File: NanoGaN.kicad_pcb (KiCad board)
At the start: 6 copper layers, 54 x 94 mm, 221 parts, among them J1 U_DC, J10 Conn_01x06, J11 Conn_01x04, J12 USB4085-GF-A, J14 Conn_01x03, J2 GND, J3 Phase_U, J4 Phase_V, J5 Phase_W, J6 FTSH-107-01-L-DV-K-TR, J7 Conn_01x03, J8 Conn_01x02, J9 Conn_01x07, Q1 IGC025S08S1, Q2 IGC025S08S1, Q3 IGC025S08S1, Q4 IGC025S08S1, Q5 IGC025S08S1, Q6 IGC025S08S1, Q7 Si2302CDS, U1 STM32H723VGTx, U10 SN74LVC1G66DCKR, U11 SN74LVC1G66DCKR, U12 LMG1205YFXR, U13 BMI323, U14 AS5047P-ATST, U15 TCAN1044VDRQ1, U16 SN74LVC1G66DCKR, U17 AD8418, U18 SN74LVC1G66DCKR, U19 NCS2220AMUT1G, U2 LMR51635XDDCR, U20 NCS2220AMUT1G, U21 NCS2220AMUT1G, U3 AMS1117, U4 AD8418, U5 LMG1205YFXR, U6 SN74LVC1G66DCKR, U7 SN74LVC1G66DCKR, U8 LMG1205YFXR, U9 AD8418, X1 8MHz

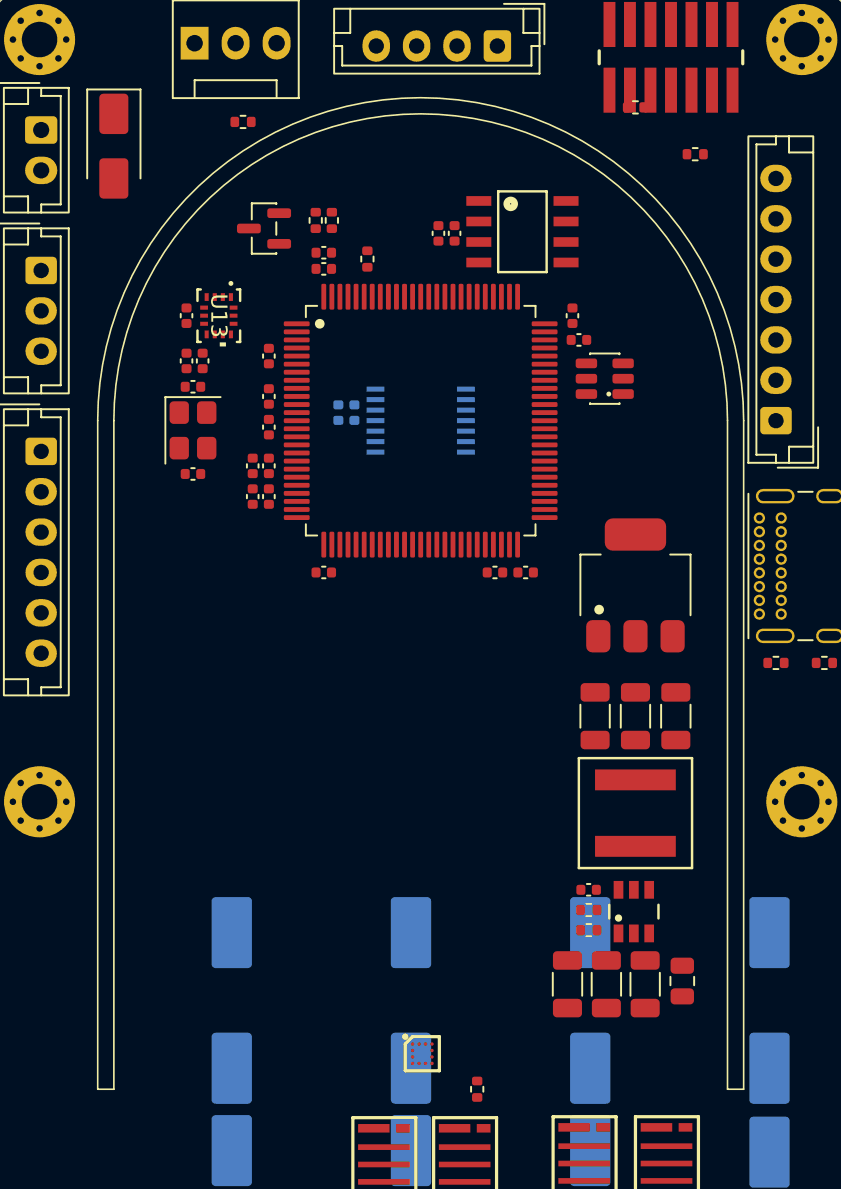
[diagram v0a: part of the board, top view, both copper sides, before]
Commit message: added cooling channel symbol, footprint and 3D model
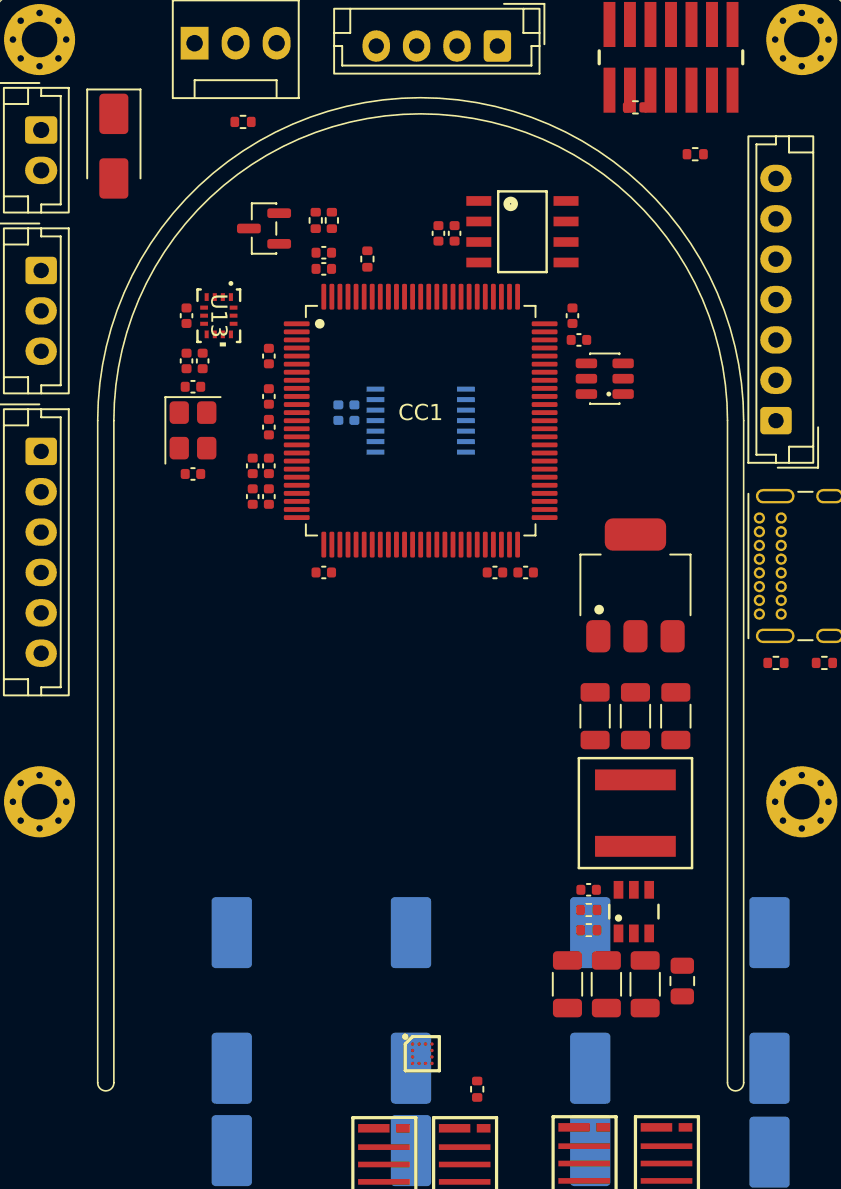
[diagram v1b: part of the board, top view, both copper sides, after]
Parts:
- added CC1: ~, NanoGaN:CoolingChannel, F.Cu at (145.2, 75.0)
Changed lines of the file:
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@@
 		)
 	)
+	(footprint "NanoGaN:CoolingChannel"
+		(layer "F.Cu")
+		(at 145.1651 75)
+		(property "Reference" "CC1"
+			(at 0 -0.5 0)
+			(unlocked yes)
+			(layer "F.SilkS")
+			(effects
+				(font
+					(size 1 1)
+					(thickness 0.1)
+				)
+			)
+		)
+		(property "Value" "~"
+			(at 0 1 0)
+			(unlocked yes)
+			(layer "F.Fab")
+			(effects
+				(font
+					(size 1 1)
+					(thickness 0.15)
+				)
+			)
+		)
+		(property "Datasheet" ""
+			(at 0 0 0)
+			(unlocked yes)
+			(layer "F.Fab")
+			(hide yes)
+			(effects
+				(font
+					(size 1 1)
+					(thickness 0.15)
+				)
+			)
+		)
+		(property "Description" ""
+			(at 0 0 0)
+			(unlocked yes)
+			(layer "F.Fab")
+			(hide yes)
+			(effects
+				(font
+					(size 1 1)
+					(thickness 0.15)
+				)
+			)
+		)
+		(sheetname "/Power/")
+		(sheetfile "power.kicad_sch")
+		(attr smd)
+		(fp_line
+			(start -20 0)
+			(end -20 41)
+			(stroke
+				(width 0.1)
+				(type solid)
+			)
+			(layer "F.SilkS")
+		)
+		(fp_line
+			(start -19 0)
+			(end -19 41)
+			(stroke
+				(width 0.1)
+				(type solid)
+			)
+			(layer "F.SilkS")
+		)
+		(fp_line
+			(start 19 0)
+			(end 19 41)
+			(stroke
+				(width 0.1)
+				(type solid)
+			)
+			(layer "F.SilkS")
+		)
+		(fp_line
+			(start 20 0)
+			(end 20 41)
+			(stroke
+				(width 0.1)
+				(type solid)
+			)
+			(layer "F.SilkS")
+		)
+		(fp_arc
+			(start -20 0)
+			(mid 0 -20)
+			(end 20 0)
+			(stroke
+				(width 0.1)
+				(type solid)
+			)
+			(layer "F.SilkS")
+		)
+		(fp_arc
+			(start -19 0)
+			(mid 0 -19)
+			(end 19 0)
+			(stroke
+				(width 0.1)
+				(type solid)
+			)
+			(layer "F.SilkS")
+		)
+		(fp_arc
+			(start -19 41)
+			(mid -19.5 41.5)
+			(end -20 41)
+			(stroke
+				(width 0.1)
+				(type default)
+			)
+			(layer "F.SilkS")
+		)
+		(fp_arc
+			(start 20 41)
+			(mid 19.5 41.5)
+			(end 19 41)
+			(stroke
+				(width 0.1)
+				(type default)
+			)
+			(layer "F.SilkS")
+		)
+		(fp_text user "${REFERENCE}"
+			(at 0 2.5 0)
+			(unlocked yes)
+			(layer "F.Fab")
+			(effects
+				(font
+					(size 1 1)
+					(thickness 0.15)
+				)
+			)
+		)
+		(embedded_fonts no)
+		(model "${KIPRJMOD}/NanoGaN_3D_models/cc_v3.step"
+			(offset
+				(xyz -23.5 23.5 -0.5)
+			)
+			(scale
+				(xyz 1 1 1)
+			)
+			(rotate
+				(xyz -0 -0 -0)
+			)
+		)
+	)
 	(footprint "Capacitor_SMD:C_0402_1005Metric"
 		(layer "F.Cu")
@@
 		)
 	)
-	(gr_line
-		(start 165.1651 75)
-		(end 165.1651 116.4)
-		(stroke
-			(width 0.1)
-			(type default)
-		)
-		(layer "F.SilkS")
-	)
-	(gr_line
-		(start 164.1651 116.4)
-		(end 165.1651 116.4)
-		(stroke
-			(width 0.1)
-			(type default)
-		)
-		(layer "F.SilkS")
-	)
-	(gr_arc
-		(start 126.1651 75)
-		(mid 145.1651 56)
-		(end 164.1651 75)
-		(stroke
-			(width 0.1)
-			(type solid)
-		)
-		(layer "F.SilkS")
-	)
-	(gr_arc
-		(start 125.1651 75)
-		(mid 145.1651 55)
-		(end 165.1651 75)
-		(stroke
-			(width 0.1)
-			(type solid)
-		)
-		(layer "F.SilkS")
-	)
-	(gr_line
-		(start 126.1651 75)
-		(end 126.1651 116.4)
-		(stroke
-			(width 0.1)
-			(type solid)
-		)
-		(layer "F.SilkS")
-	)
-	(gr_line
-		(start 126.1651 116.4)
-		(end 125.1651 116.4)
-		(stroke
-			(width 0.1)
-			(type default)
-		)
-		(layer "F.SilkS")
-	)
-	(gr_line
-		(start 164.1651 75)
-		(end 164.1651 116.4)
-		(stroke
-			(width 0.1)
-			(type default)
-		)
-		(layer "F.SilkS")
-	)
-	(gr_line
-		(start 125.1651 75)
-		(end 125.1651 116.4)
-		(stroke
-			(width 0.1)
-			(type solid)
-		)
-		(layer "F.SilkS")
-	)
 	(gr_arc

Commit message: added the first draft of the layout
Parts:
- removed C102, C104: 1u, Capacitor_SMD:C_0402_1005Metric
- removed C103, C105: 100n, Capacitor_SMD:C_0402_1005Metric
- removed C96, C97, C98, C99: 1n, Capacitor_SMD:C_0201_0603Metric
- removed R28: 1m, NanoGaN:RES_00FEA_VIS-L
- removed R30, R32: 10k, Resistor_SMD:R_0603_1608Metric
- removed R7: 10k, Resistor_SMD:R_0402_1005Metric
- removed U10, U11, U16, U18: SN74LVC1G66DCKR, NanoGaN:DCK5
- removed U17, U9: AD8418, Package_SO:SOIC-8_3.9x4.9mm_P1.27mm
- added C67: 100n, Capacitor_SMD:C_0805_2012Metric, F.Cu at (152.7, 134.9)
- added C68: 1u, Capacitor_SMD:C_1206_3216Metric, F.Cu at (167.7, 128.1)
- added MH7: M3, MountingHole:MountingHole_3.2mm_M3_Pad_Via, F.Cu at (168.8, 142.6)
- C100: value 1u -> 100n
- C11, C12, C13, C14, C27, C35: value 150u -> 470u; footprint Capacitor_SMD:CP_Elec_10x10.5 -> Capacitor_THT:CP_Radial_D12.5mm_P5.00mm
- C18, C36, C85, C87: footprint Capacitor_SMD:C_0201_0603Metric -> Capacitor_SMD:C_0402_1005Metric
- C24, C25, C33, C38, C89: moved to B.Cu
- C26: value 1u -> 100n; moved to B.Cu
- C28, C39, C91: value 1n -> 100p; footprint Capacitor_SMD:C_0201_0603Metric -> Capacitor_SMD:C_0402_1005Metric; moved to B.Cu
- C37: value 1u -> 4u7
- C40: value 15n -> 4u7
- C44, C81: value 150u -> 100n; footprint Capacitor_SMD:CP_Elec_10x10.5 -> Capacitor_SMD:C_0805_2012Metric; moved to F.Cu
- C50: footprint Capacitor_SMD:C_0402_1005Metric -> Capacitor_SMD:C_0805_2012Metric
- C88: value 1u -> 100n; footprint Capacitor_SMD:C_0402_1005Metric -> Capacitor_SMD:C_0805_2012Metric
- C90: value 15n -> 100n; footprint Capacitor_SMD:C_0402_1005Metric -> Capacitor_SMD:C_0805_2012Metric
- C92: value 15n -> 100n
- J1: value U_DC -> XT60-M; footprint TerminalBlock_Wuerth:Wuerth_REDCUBE-THR_WP-THRBU_74650073_THR -> NanoGaN:AMASS_XT60-M
- J2: value GND -> XT60-M; footprint TerminalBlock_Wuerth:Wuerth_REDCUBE-THR_WP-THRBU_74650073_THR -> NanoGaN:AMASS_XT60-M
- MH1, MH2, MH3, MH4, MH5, MH6: value M2 -> M3; footprint MountingHole:MountingHole_2.2mm_M2_Pad_Via -> MountingHole:MountingHole_3.2mm_M3_Pad_Via
- R11, R21: value 1m -> 10k; footprint NanoGaN:RES_00FEA_VIS-L -> Resistor_SMD:R_0402_1005Metric
- U4: value AD8418 -> ACS37030LLZATR-065B3; footprint Package_SO:SOIC-8_3.9x4.9mm_P1.27mm -> NanoGaN:ACS37030LLZATR020B3; moved to B.Cu
- U6, U7: value SN74LVC1G66DCKR -> ACS37030LLZATR-065B3; footprint NanoGaN:DCK5 -> NanoGaN:ACS37030LLZATR020B3; moved to B.Cu
- moved U12 148.0 mm to (131.4, 126.1), turned to 90 degrees
- moved R5 147.7 mm to (151.5, 139.0)
- moved C18 145.7 mm to (151.5, 138.0)
- moved R23 143.3 mm to (129.3, 128.4), turned to -90 degrees
- moved C91 141.8 mm to (121.9, 132.3), turned to 90 degrees
- moved R4 141.2 mm to (151.0, 141.0), turned to 90 degrees
- moved R25 140.3 mm to (130.3, 128.4), turned to 90 degrees
- moved R22 140.1 mm to (134.4, 128.4), turned to -90 degrees
- moved C41 140.0 mm to (128.3, 126.1), turned to -90 degrees
- moved R27 139.9 mm to (136.4, 139.0)
- moved R24 139.6 mm to (132.4, 128.4), turned to 90 degrees
- moved Q6 139.3 mm to (127.9, 132.8), turned to -90 degrees
- moved Q5 139.2 mm to (133.0, 132.8), turned to -90 degrees
- moved C89 139.2 mm to (123.7, 129.5), turned to 180 degrees
- moved C43 138.1 mm to (129.3, 126.1), turned to -90 degrees
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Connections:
- net /MCU/BOOT0 renamed BOOT0
- C100 pad 1: +3V3A -> +3V3
- C101 pad 1: +3V3A -> +3V3
- C24 pad 1: +3V3A -> +3V3
- C24 pad 2: AGND -> PGND
- C25 pad 1: Net-(U16-A) -> /HalfBridgeU/I_CURR_SENS-
- C25 pad 2: /HalfBridgeU/U_PHASE_SENS -> PGND
- C26 pad 1: +3V3A -> /HalfBridgeV/I_CURR_SENS-
- C26 pad 2: AGND -> PGND
- C28 pad 1: /HalfBridgeU/I_CURR_SENS -> /HalfBridgeU/I_CURR_SENS+
- C28 pad 2: AGND -> PGND
- C33 pad 1: Net-(U7-A) -> /HalfBridgeW/I_CURR_SENS-
- C33 pad 2: /HalfBridgeV/U_PHASE_SENS -> PGND
- C37 pad 1: +3V3A -> +3V3
- C37 pad 2: AGND -> GND
- C38 pad 1: +3V3A -> +3V3
- C38 pad 2: AGND -> PGND
- C39 pad 1: /HalfBridgeV/I_CURR_SENS -> /HalfBridgeV/I_CURR_SENS+
- C39 pad 2: AGND -> PGND
- C40 pad 1: /HalfBridgeV/I_CURR_SENS -> +3V3
- C40 pad 2: Net-(U10-A) -> GND
- C50 pad 1: Net-(U11-A) -> U_DC
- C50 pad 2: /HalfBridgeW/U_PHASE_SENS -> PGND
- C88 pad 1: +3V3A -> U_DC
- C88 pad 2: AGND -> PGND
- C89 pad 1: +3V3A -> +3V3
- C89 pad 2: AGND -> PGND
- C90 pad 1: /HalfBridgeU/I_CURR_SENS -> U_DC
- C90 pad 2: Net-(U6-A) -> PGND
- C91 pad 1: /HalfBridgeW/I_CURR_SENS -> /HalfBridgeW/I_CURR_SENS+
- C91 pad 2: AGND -> PGND
- C92 pad 1: /HalfBridgeW/I_CURR_SENS -> +3V3
- C92 pad 2: Net-(U18-A) -> AGND
- C95 pad 1: /HalfBridgeU/DAC_OCP_P -> /HalfBridgeU/DAC_OCP_N
- MH3 pad 1: PGND -> GND
- R11 pad 1: /HalfBridgeU/HS -> /Connectors/EXT_TEMP2
- R11 pad 2: /HalfBridgeU/PHASE -> GND
- R21 pad 1: /HalfBridgeV/HS -> /Connectors/EXT_TEMP1
- R21 pad 2: /HalfBridgeV/PHASE -> GND
- U1 pad 22: unconnected-(U1-PA0-Pad22) -> /HalfBridgeU/U_PHASE_SENS
- U1 pad 23: unconnected-(U1-PA1-Pad23) -> /HalfBridgeV/U_PHASE_SENS
- U1 pad 24: unconnected-(U1-PA2-Pad24) -> /HalfBridgeW/U_PHASE_SENS
- U1 pad 30: /HalfBridgeW/I_CURR_SENS -> /HalfBridgeU/I_CURR_SENS+
- U1 pad 31: /HalfBridgeW/U_PHASE_SENS -> /HalfBridgeU/I_CURR_SENS-
- U1 pad 32: /HalfBridgeV/U_PHASE_SENS -> /HalfBridgeV/I_CURR_SENS+
- U1 pad 33: /HalfBridgeV/I_CURR_SENS -> /HalfBridgeV/I_CURR_SENS-
- U1 pad 34: /HalfBridgeU/I_CURR_SENS -> /HalfBridgeW/I_CURR_SENS-
- U1 pad 35: /HalfBridgeU/U_PHASE_SENS -> /HalfBridgeW/I_CURR_SENS+
- U1 pad 37: /HalfBridgeU/EN_FILTER_I -> unconnected-(U1-PE7-Pad37)
- U1 pad 7: unconnected-(U1-PC13-Pad7) -> /Connectors/HALL1
- U1 pad 8: unconnected-(U1-PC14-Pad8) -> /Connectors/HALL2
- U1 pad 81: FDCAN1_RX -> /MCU/UART4_RX
- U1 pad 82: FDCAN1_TX -> /MCU/UART4_TX
- U1 pad 83: FDCAN1_STB -> unconnected-(U1-PD2-Pad83)
- U1 pad 85: unconnected-(U1-PD4-Pad85) -> FDCAN1_STB
- U1 pad 9: unconnected-(U1-PC15-Pad9) -> /Connectors/HALL3
- U1 pad 90: /Connectors/SERVO -> unconnected-(U1-PB4(NJTRST)-Pad90)
- U1 pad 91: /Connectors/SERVO -> unconnected-(U1-PB5-Pad91)
- U1 pad 92: /Connectors/VCP_RX -> unconnected-(U1-PB6-Pad92)
- U1 pad 93: /Connectors/VCP_TX -> unconnected-(U1-PB7-Pad93)
- U1 pad 95: unconnected-(U1-PB8-Pad95) -> FDCAN1_RX
- U1 pad 96: /Connectors/FAN_PWM -> FDCAN1_TX
- U13 pad 1: SPI4_MISO -> SPI2_MISO
- U13 pad 12: SPI4_NSS -> SPI2_NSS
- U13 pad 13: SPI4_SCK -> SPI2_SCK
- U13 pad 14: SPI4_MOSI -> SPI2_MOSI
- U14 pad 1: SPI2_NSS -> SPI4_NSS
- U14 pad 2: SPI2_SCK -> SPI4_SCK
- U14 pad 3: SPI2_MISO -> SPI4_MISO
- U14 pad 4: SPI2_MOSI -> SPI4_MOSI
- U19 pad 2: /HalfBridgeU/I_CURR_SENS -> /HalfBridgeU/I_CURR_SENS+
- U19 pad 6: /HalfBridgeU/I_CURR_SENS -> /HalfBridgeU/I_CURR_SENS+
- U19 pad 8: +3V3A -> +3V3
- U20 pad 2: /HalfBridgeV/I_CURR_SENS -> /HalfBridgeV/I_CURR_SENS+
- U20 pad 6: /HalfBridgeV/I_CURR_SENS -> /HalfBridgeV/I_CURR_SENS+
- U20 pad 8: +3V3A -> +3V3
- U21 pad 2: /HalfBridgeW/I_CURR_SENS -> /HalfBridgeW/I_CURR_SENS+
- U21 pad 6: /HalfBridgeW/I_CURR_SENS -> /HalfBridgeW/I_CURR_SENS+
- U21 pad 8: +3V3A -> +3V3
- U4 pad 1: /HalfBridgeU/PHASE -> /HalfBridgeU/HS
- U4 pad 2: AGND -> /HalfBridgeU/PHASE
- U4 pad 3: AGND -> PGND
- U4 pad 4: unconnected-(U4-NC-Pad4) -> /HalfBridgeU/I_CURR_SENS-
- U4 pad 5: /HalfBridgeU/I_CURR_SENS -> /HalfBridgeU/I_CURR_SENS+
- U4 pad 6: +3V3A -> +3V3
- U6 pad 1: Net-(U6-A) -> /HalfBridgeV/HS
- U6 pad 2: AGND -> /HalfBridgeV/PHASE
- U6 pad 4: /HalfBridgeU/EN_FILTER_I -> /HalfBridgeV/I_CURR_SENS-
- U6 pad 5: +3V3A -> /HalfBridgeV/I_CURR_SENS+
- U7 pad 1: Net-(U7-A) -> /HalfBridgeW/HS
- U7 pad 2: PGND -> /HalfBridgeW/PHASE
- U7 pad 4: /HalfBridgeU/EN_FILTER_U -> /HalfBridgeW/I_CURR_SENS-
- U7 pad 5: +3V3A -> /HalfBridgeW/I_CURR_SENS+
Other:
- board size 54 x 94 mm -> 60 x 100 mm
- board text added: "JLCJLCJLC"

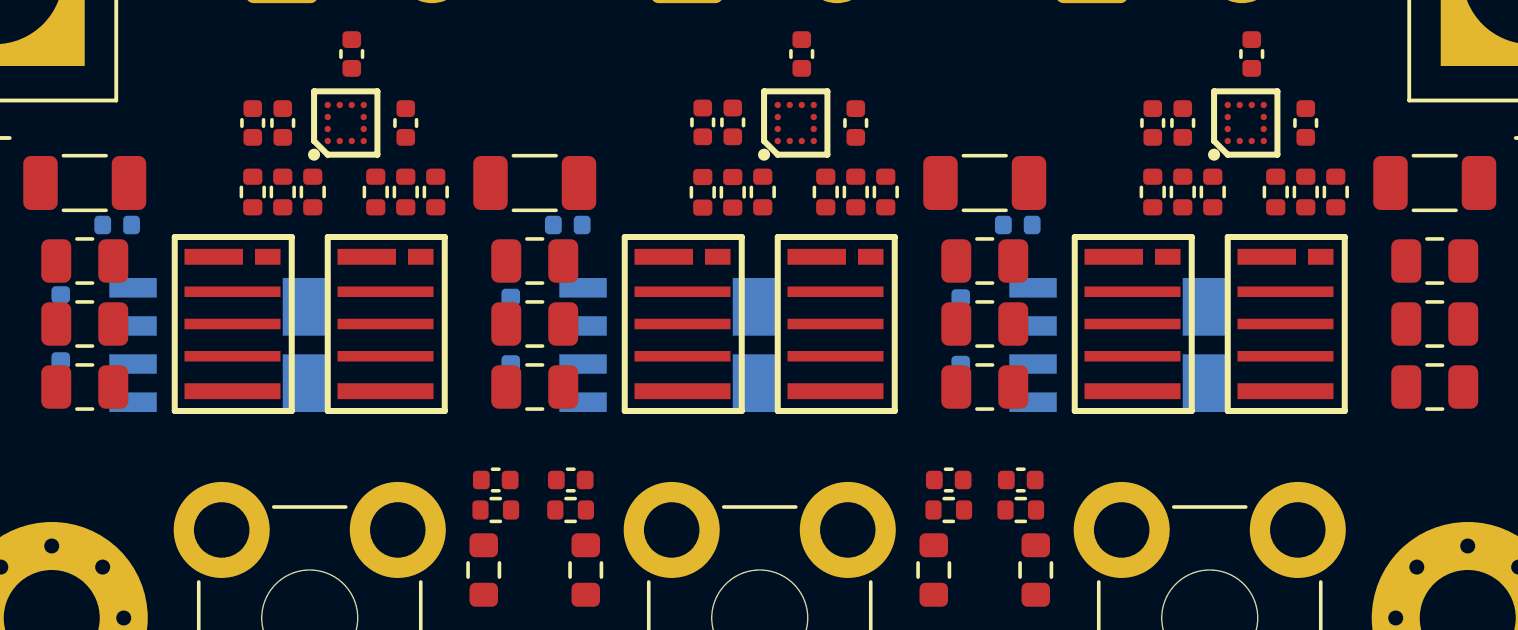
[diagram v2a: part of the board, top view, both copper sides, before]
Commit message: added heatsinks and updated cooling channel
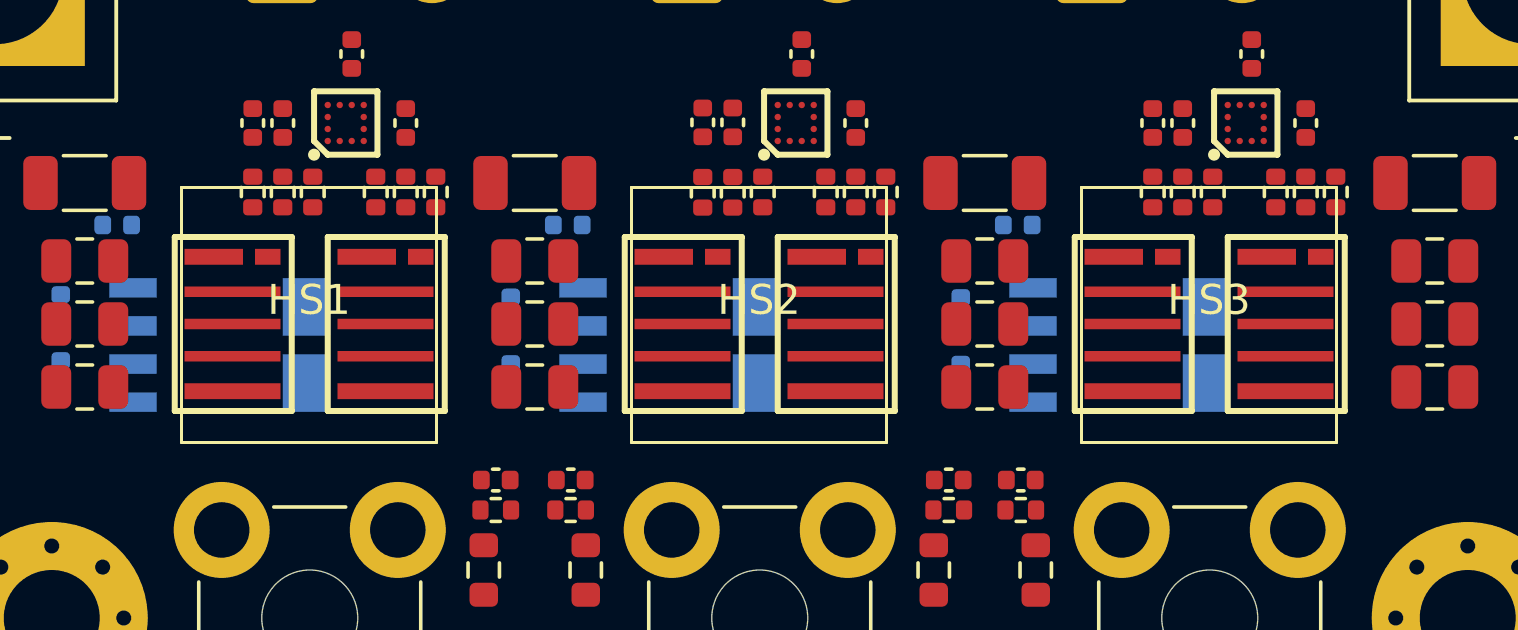
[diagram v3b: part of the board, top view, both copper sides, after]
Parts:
- added HS1: Heatsink, NanoGaN:HSB01-080808, F.Cu at (130.1, 132.5)
- added HS2: Heatsink, NanoGaN:HSB01-080808, F.Cu at (145.1, 132.5)
- added HS3: Heatsink, NanoGaN:HSB01-080808, F.Cu at (160.1, 132.5)

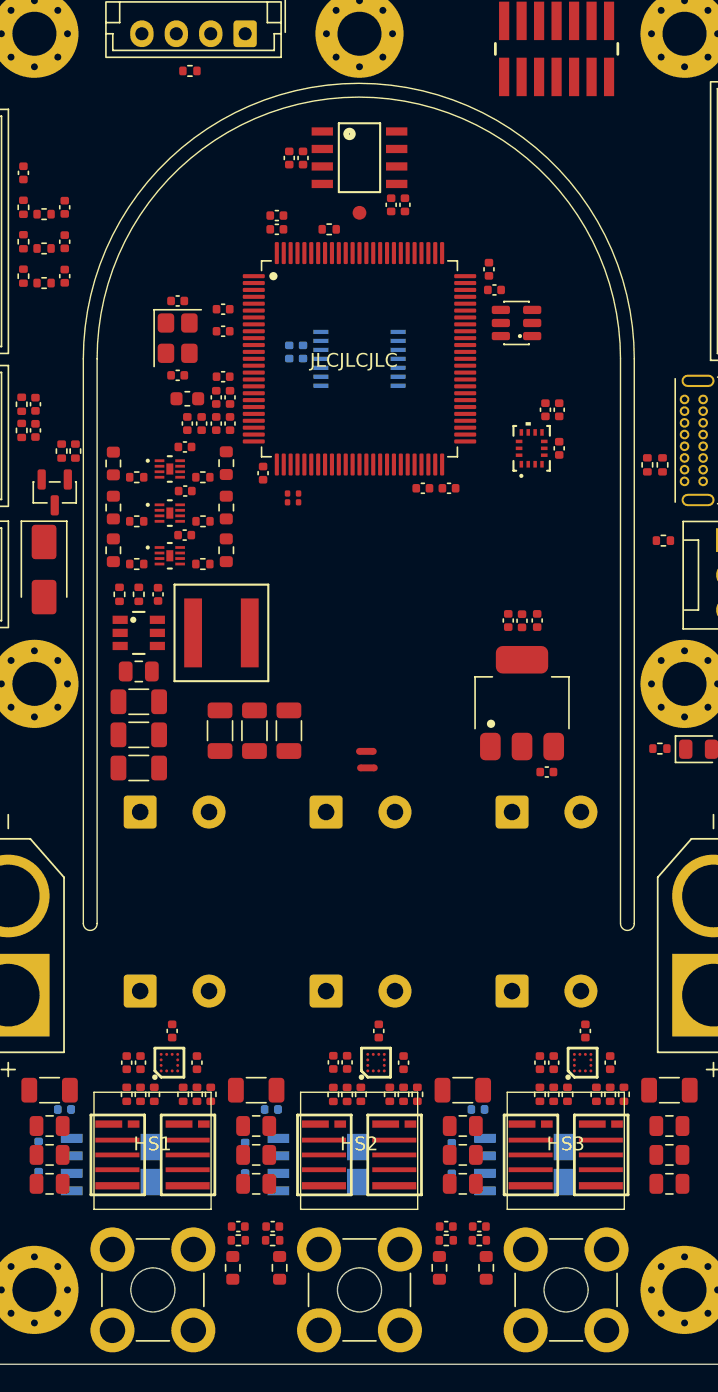
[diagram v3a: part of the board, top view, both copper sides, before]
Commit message: small footprint update for cooling channel and heatsinks
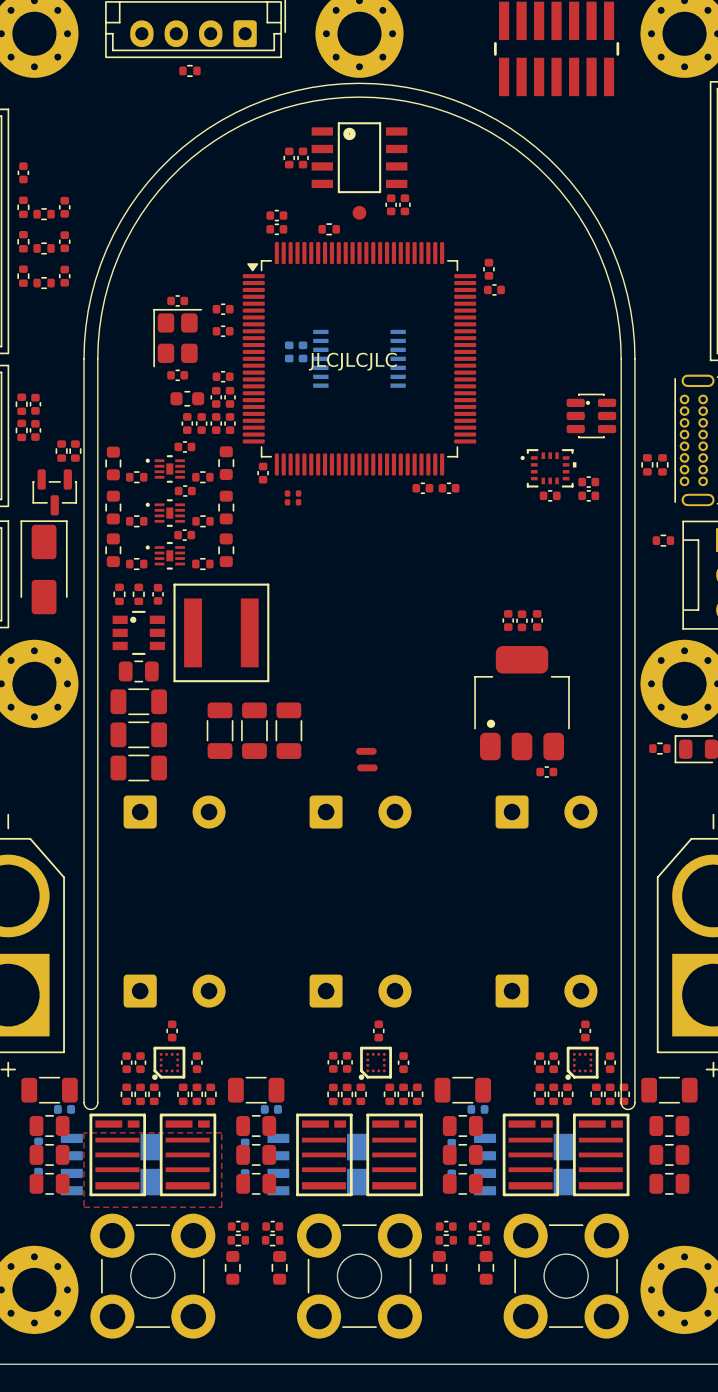
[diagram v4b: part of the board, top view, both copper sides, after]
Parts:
- moved D2 8.67 mm to (162.0, 79.2), turned to 0 degrees
- moved C54 6.61 mm to (161.8, 85.0), turned to 0 degrees
- moved C57 6.12 mm to (161.8, 84.0), turned to 0 degrees
- moved C56 3.51 mm to (159.0, 85.0), turned to 0 degrees
- moved U13 1.98 mm to (159.0, 83.0), turned to 0 degrees
- moved J3 1.00 mm to (160.2, 141.6)
- moved J4 1.00 mm to (145.2, 141.6)
- moved J5 1.00 mm to (130.2, 141.6)
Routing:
- added copper zone on F.Cu, net /HalfBridgeW/HS
